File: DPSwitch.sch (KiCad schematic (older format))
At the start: 44 parts, among them J1 USB_OTG, J2 USB_OTG, J3 DP_47272, J4 DP_47272, J5 DP_47272, J6 USB_A, SW1 SEL_A, SW2 SEL_B, U1 HD3SS215, U2 74LVC2G00DC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

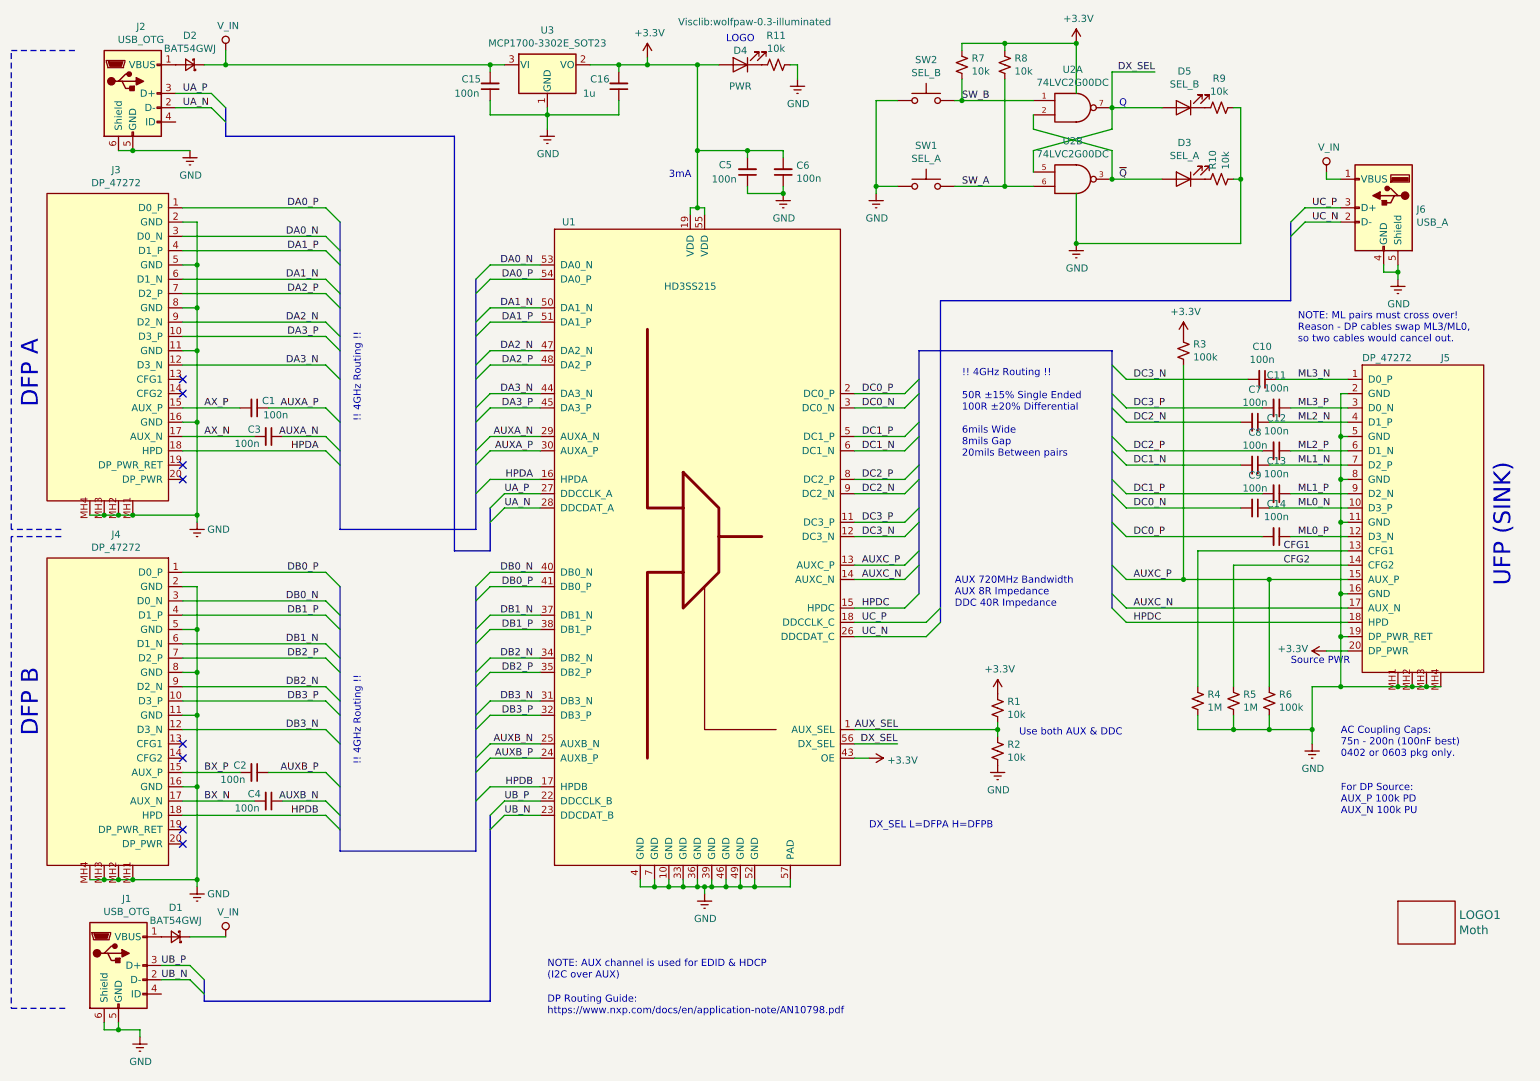
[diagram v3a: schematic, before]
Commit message: Add testpads, 0R resistors to allow reconfiguration, and OSHW logo
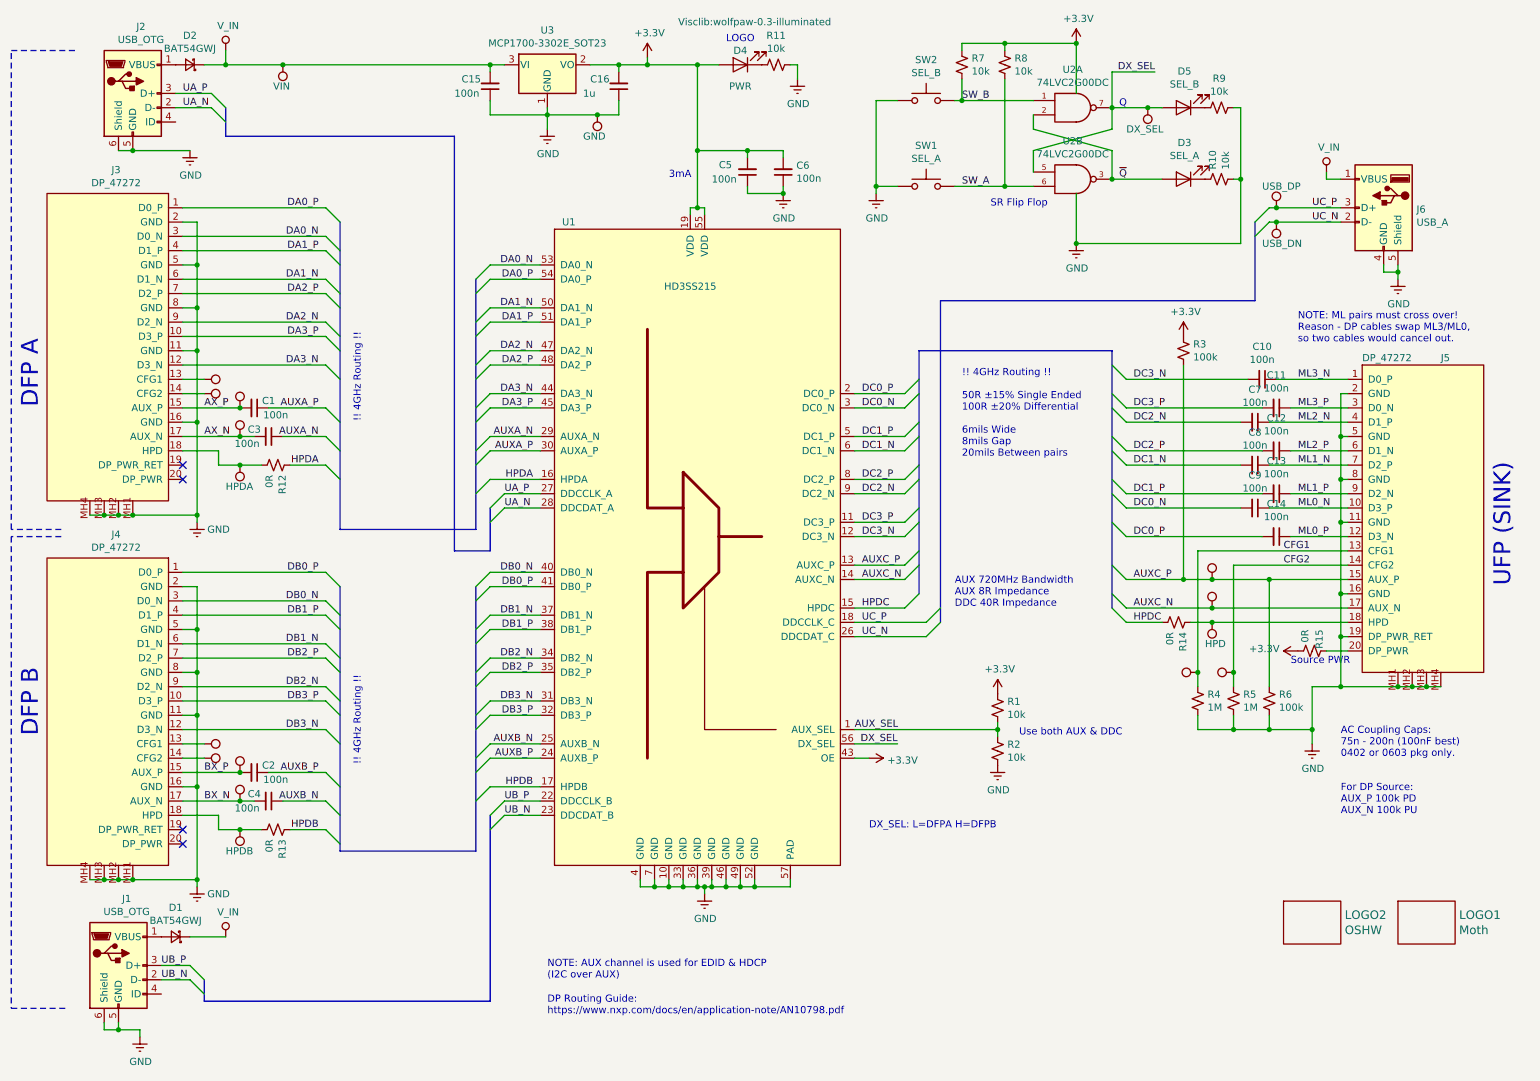
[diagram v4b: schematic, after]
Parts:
- added LOGO2: OSHW, SFAesthetics:OSHW-LOGO-M, symbol visclib:Logo
- added R12, R13, R14, R15: 0R, Resistors_SMD:R_0603_HandSoldering, symbol device:R_Small_US
- added TP1: CFG1A, Visclib:TP-1MM, symbol visclib:TP
- added TP10: HPDB, Visclib:TP-1MM, symbol visclib:TP
- added TP11: VIN, Visclib:TP-1MM, symbol visclib:TP
- added TP13: DX_SEL, Visclib:TP-1MM, symbol visclib:TP
- added TP14: CFG1, Visclib:TP-1MM, symbol visclib:TP
- added TP15: AUX_P, Visclib:TP-1MM, symbol visclib:TP
- added TP16: AUX_N, Visclib:TP-1MM, symbol visclib:TP
- added TP17: HPD, Visclib:TP-1MM, symbol visclib:TP
- added TP18: CFG2, Visclib:TP-1MM, symbol visclib:TP
- added TP19: USB_DP, Visclib:TP-1MM, symbol visclib:TP
- added TP2: CFG2A, Visclib:TP-1MM, symbol visclib:TP
- added TP20: USB_DN, Visclib:TP-1MM, symbol visclib:TP
- added TP21: GND, Visclib:TP-1MM, symbol visclib:TP
- added TP3: CFG1B, Visclib:TP-1MM, symbol visclib:TP
- added TP4: CFG2B, Visclib:TP-1MM, symbol visclib:TP
- added TP5: AUXA_P, Visclib:TP-1MM, symbol visclib:TP
- added TP6: AUXA_N, Visclib:TP-1MM, symbol visclib:TP
- added TP7: HPDA, Visclib:TP-1MM, symbol visclib:TP
- added TP8: AUXB_P, Visclib:TP-1MM, symbol visclib:TP
- added TP9: AUXB_N, Visclib:TP-1MM, symbol visclib:TP
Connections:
- net +3V3: now also R15.2; no longer J5.20 (DP_PWR)
- net AUXC_N: now also TP16.1
- net AUXC_P: now also TP15.1
- net AX_N: now also TP6.1
- net AX_P: now also TP5.1
- net BX_N: now also TP9.1
- net BX_P: now also TP8.1
- net CFG1: now also TP14.1
- net CFG2: now also TP18.1
- net DX_SEL: now also TP13.1
- net GND: now also TP21.1
- net HPDA: now also R12.1; no longer J3.18 (HPD)
- net HPDB: now also R13.1; no longer J4.18 (HPD)
- net HPDC: now also R14.2; no longer J5.18 (HPD)
- net UC_N: now also TP20.1
- net UC_P: now also TP19.1
- net VDD: now also TP11.1
- net at J3.13 (CFG1): now also TP1.1
- net at J3.14 (CFG2): now also TP2.1
- net at J4.13 (CFG1): now also TP3.1
- net at J4.14 (CFG2): now also TP4.1
- new net: J3.18 (HPD), R12.2, TP7.1
- new net: J5.18 (HPD), R14.1, TP17.1
- new net: J5.20 (DP_PWR), R15.1
- new net: J4.18 (HPD), R13.2, TP10.1
- no-connect marks 8 -> 4
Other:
- note added: "DX_SEL: L=DFPA H=DFPB"
- note added: "SR Flip Flop"
- note removed: "DX_SEL L=DFPA H=DFPB"
